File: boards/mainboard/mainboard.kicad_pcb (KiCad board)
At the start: 2 copper layers, 107.3 x 68.6 mm, 322 parts, among them J1001 FL2_CS, J1002 FL2_SCK, J1003 FL2_MISO, J1004 FL2_MOSI, J101 Powerboard <-> Mainboard, J102 Temperature & Pressure, J103 Camera board, J104 temp_SCL, J105 temp_SDA, J106 pres_SCL, J107 pres_SDA, J108 RasPi_TX, J109 RasPi_RX, J110 3V3, J1101 FL1_CS, J1102 FL1_SCK, J1103 FL1_MISO, J1104 FL1_MOSI, J111 GND, J112 M3, J113 M3, J114 M3, J115 M3, J116 M3, J117 M3, J1201 ENC1_A, J1202 ENC1_B, J1203 ENC2_A, J1204 ENC2_B, J1205 ENC3_A, J1206 ENC3_B, J201 RTD_31-36, J202 T_SPI1_SCK, J203 T_SPI1_MISO, J204 T_SPI1_MOSI, J205 T_SPI2_SCK, J206 T_SPI2_MISO, J207 T_SPI2_MOSI, J208 T_SPI1_CS1, J209 T_SPI1_CS2, J210 T_SPI1_CS3, J211 T_SPI2_CS1, J212 T_SPI2_CS2, J213 T_SPI2_CS3, P901 DEBUG, P902 SWD, SW101 SW_PUSH, SW102 SW_PUSH, SW901 RESET, SW902 BOOT0, U1001 SST26VF064B, U101 LM1117-3.3, U1101 SST26VF064B, U1201 Heat probe encoder, U1202 DS26LV32AT, U1203 DS26LV32AT, U201 RTD_20-30, U202 RTD_1-19, U301 LTC2984, U401 LTC2984, U501 LTC2984, U601 LTC2984, U701 LTC2984, U801 LTC2984, U901 STM32F429ZITx, X901 XO53

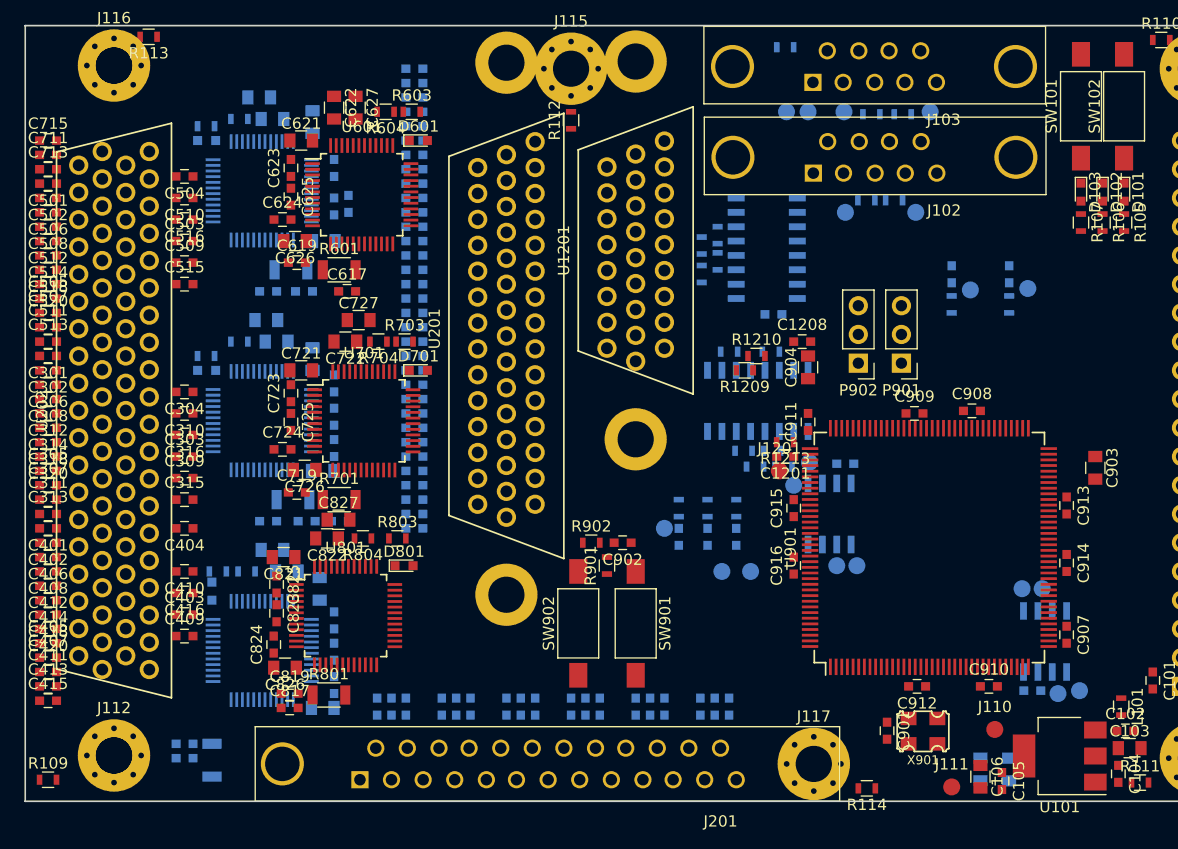
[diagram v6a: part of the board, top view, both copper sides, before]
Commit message: [mainboard] first traces routed, some pins in schematic swapped
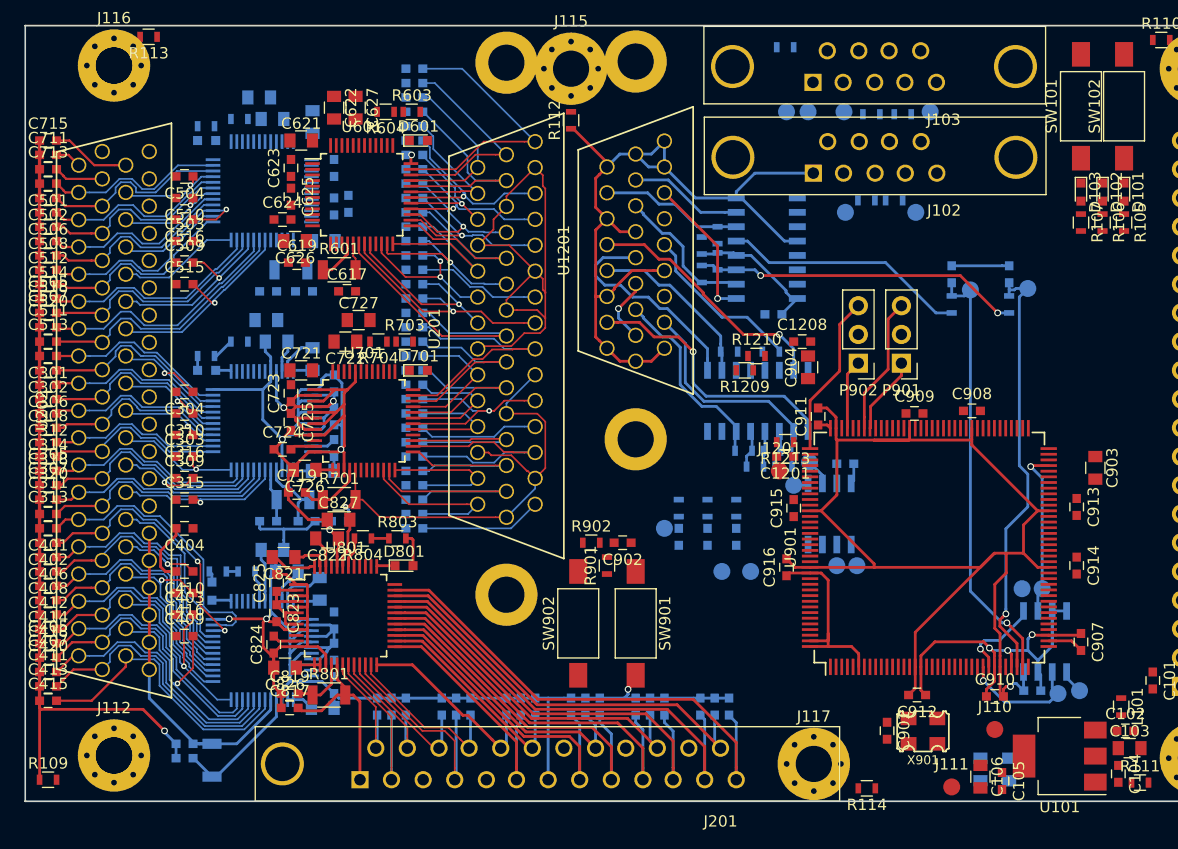
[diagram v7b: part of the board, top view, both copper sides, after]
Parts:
- moved C907 1.42 mm to (83.8, 104.0)
- moved C910 1.04 mm to (76.2, 108.8)
- moved C911 1.01 mm to (60.6, 84.1)
- moved C914 0.92 mm to (83.4, 97.3)
- moved C913 0.90 mm to (83.4, 92.1)
- moved C912 0.76 mm to (69.3, 108.7)
- moved C916 0.65 mm to (57.8, 97.4)
- moved C825 0.14 mm to (12.7, 98.8), turned to 90 degrees
- turned C325 to 270 degrees
- turned C425 to 270 degrees
- turned C812 to 90 degrees
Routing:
- net GND: track 0.00 -> 486.4 mm, vias 0 -> 9
- net +3V3: track 0.00 -> 126.5 mm, vias 0 -> 5
- net /Mainboard_Temp_Sensors/T5_RTD1_A: track 0.00 -> 49.2 mm
- net /Mainboard_Temp_Sensors/T6_RTD6_D: track 0.00 -> 45.0 mm
- net /Mainboard_Temp_Sensors/T4_RTD1_A: track 0.00 -> 43.3 mm, vias 0 -> 1
- net /Mainboard_Temp_Sensors/T6_RTD6_B: track 0.00 -> 41.5 mm
- net /Mainboard_Temp_Sensors/T6_RTD5_D: track 0.00 -> 39.0 mm
- net /Heat_Probe_Encoder/ENC3_A: track 0.00 -> 38.6 mm, vias 0 -> 1
- net /Heat_Probe_Encoder/ENC3_B: track 0.00 -> 38.5 mm, vias 0 -> 1
- net /Mainboard_Temp_Sensors/T6_RTD6_C: track 0.00 -> 37.5 mm
- net /Mainboard_Temp_Sensors/T6_RTD5_B: track 0.00 -> 35.5 mm
- net /Mainboard_Temp_Sensors/T6_RTD4_D: track 0.00 -> 32.7 mm
- net /Mainboard_Temp_Sensors/T6_RTD5_C: track 0.00 -> 31.4 mm
- net /Mainboard_Temp_Sensors/T1_RTD1_A: track 0.00 -> 30.8 mm
- net /Mainboard_Temp_Sensors/T6_RTD4_B: track 0.00 -> 29.4 mm
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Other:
- net class T_PT-100 added: clearance 0.15, trace_width 0.15, via_dia 0.5, via_drill 0.25
- rule via_min_drill: 0.3 -> 0.2

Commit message: [mainboard] about half of the traces routed
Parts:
- moved R901 34.5 mm to (74.2, 109.5)
- moved C902 32.8 mm to (72.8, 109.6), turned to 270 degrees
- moved R1217 3.93 mm to (74.0, 76.1), turned to 180 degrees
- moved C1205 3.56 mm to (73.9, 71.5)
- moved J1205 3.30 mm to (75.8, 72.9)
- moved J1206 1.27 mm to (74.0, 74.2)
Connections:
- J1101 pad 1: /Mainboard microcontroller/Mainboard_Flash_1/CS -> /Mainboard microcontroller/Flash1_CS
- U1101 pad 1: /Mainboard microcontroller/Mainboard_Flash_1/CS -> /Mainboard microcontroller/Flash1_CS
- U901 pad 37: (no net) -> /Mainboard microcontroller/Flash1_CS
- U901 pad 44: /Mainboard microcontroller/Mainboard_Flash_1/CS -> (no net)
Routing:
- net /temperature_SDA: track 0.00 -> 84.0 mm, vias 0 -> 1
- net GND: track 486.4 -> 566.7 mm
- net /temperature_SCL: track 0.00 -> 75.6 mm, vias 0 -> 1
- net /RasPi_TX: track 0.00 -> 59.6 mm, vias 0 -> 1
- net /RasPi_RX: track 0.00 -> 57.9 mm, vias 0 -> 1
- net /pressure_SCL: track 0.00 -> 53.3 mm
- net /pressure_SDA: track 0.00 -> 49.0 mm, vias 0 -> 1
- net /Mainboard microcontroller/NRST: track 0.00 -> 39.1 mm, vias 0 -> 2
- net +3V3: track 126.5 -> 154.7 mm, vias 5 -> 6
- net /Mainboard_Temp_Sensors/T4_RTD2_B: track 10.8 -> 27.2 mm
- net /Mainboard microcontroller/Mainboard_Flash_2/SCK: track 0.00 -> 15.6 mm, vias 0 -> 1
- net +5V: track 5.84 -> 16.3 mm
- net /Mainboard microcontroller/Mainboard_Flash_2/MOSI: track 0.00 -> 7.34 mm, vias 0 -> 1
- net /5V_filtered: track 0.00 -> 6.59 mm
- net /Mainboard microcontroller/Flash1_CS: track 0.00 -> 5.83 mm, vias 0 -> 1
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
